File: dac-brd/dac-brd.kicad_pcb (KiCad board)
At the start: 2 copper layers, 51 x 53 mm, 19 parts, among them J1 HTR, J2 I2C, J3 UART, U1 REF5030ID, U2 DAC5578xPW, U3 DAC5578xPW

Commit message: Modified DAC, AMP v2 and Mezzanine to support AMP v3. Finished AMP v3 design.
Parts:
- U1: value REF5030ID -> REF5020ID
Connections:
- net /LED_PWM renamed /EN
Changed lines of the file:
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@@
 	(net 16 "+5V")
 	(net 17 "unconnected-(A1-VSYS-Pad39)")
-	(net 18 "/LED_PWM")
+	(net 18 "/EN")
 	(net 19 "unconnected-(U1-Temp-Pad3)")
 	(net 20 "unconnected-(U1-DNC-Pad1)")
@@
 			(layers "*.Cu" "*.Mask")
 			(remove_unused_layers no)
-			(net 18 "/LED_PWM")
+			(net 18 "/EN")
 			(pinfunction "GPIO17")
 			(pintype "bidirectional")
@@
 			(layers "F.Cu" "F.Mask")
 			(roundrect_rratio 0.5)
-			(net 18 "/LED_PWM")
+			(net 18 "/EN")
 			(pinfunction "GPIO17")
 			(pintype "bidirectional")
@@
 			(layers "*.Cu" "*.Mask")
 			(remove_unused_layers no)
-			(net 18 "/LED_PWM")
+			(net 18 "/EN")
 			(pinfunction "Pin_33")
 			(pintype "passive")
@@
 			)
 		)
-		(property "Value" "REF5030ID"
+		(property "Value" "REF5020ID"
 			(at 0 3.4 90)
 			(layer "F.Fab")
@@
 			)
 		)
-		(property "Description" "3V 0.05% 10mA Low Noise Precision Voltage Reference, SO-8"
+		(property "Description" "2.048V 0.05% 10mA Low Noise Precision Voltage Reference, SO-8"
 			(at 0 0 90)
 			(layer "F.Fab")

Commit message: Final review with Joe
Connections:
- C6 pad 1: +5V -> +3V3
- U1 pad 2: +5V -> +3V3
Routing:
- net +5V: track 46.4 -> 0.00 mm, vias 1 -> 0
- net +3V3: track 28.0 -> 34.5 mm
- net GND: track 4.57 -> 5.79 mm
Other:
- board text added: "EN"
- board text removed: "LED"

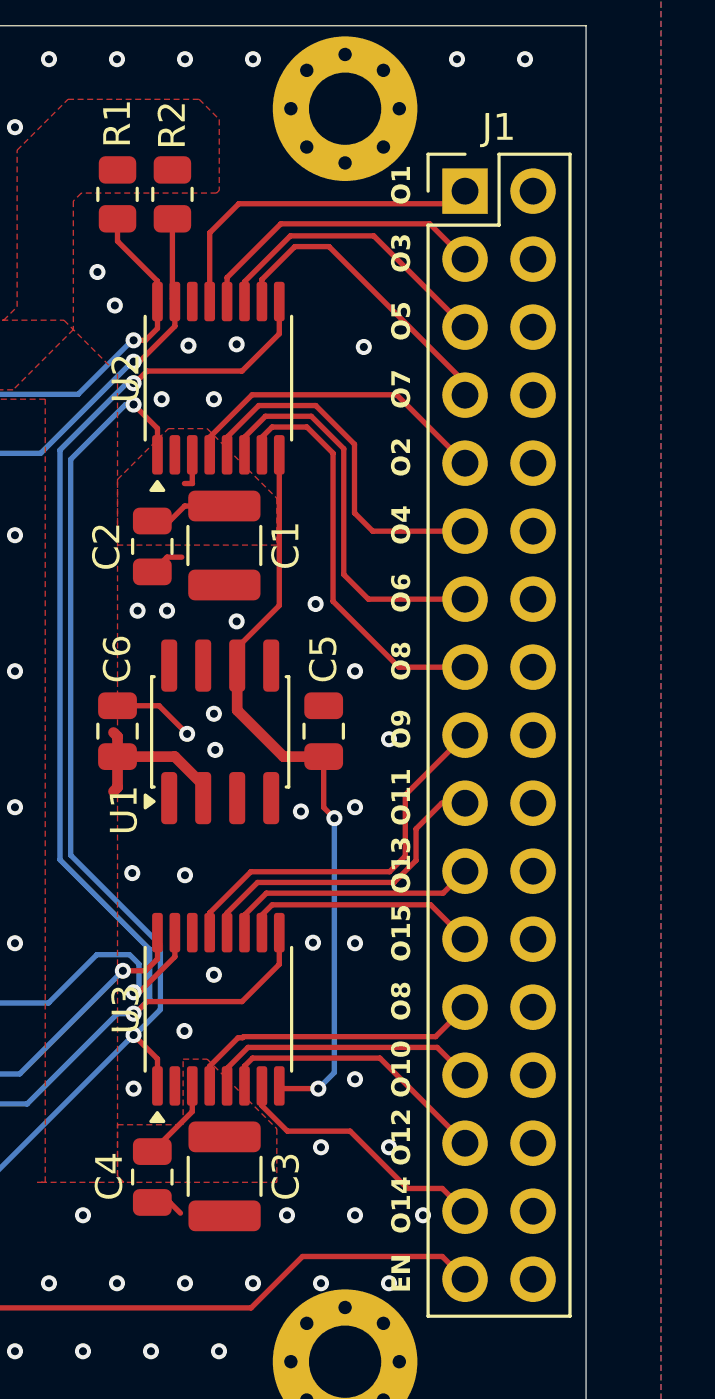
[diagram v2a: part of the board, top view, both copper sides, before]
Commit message: Tested DAC and partially tested INA233
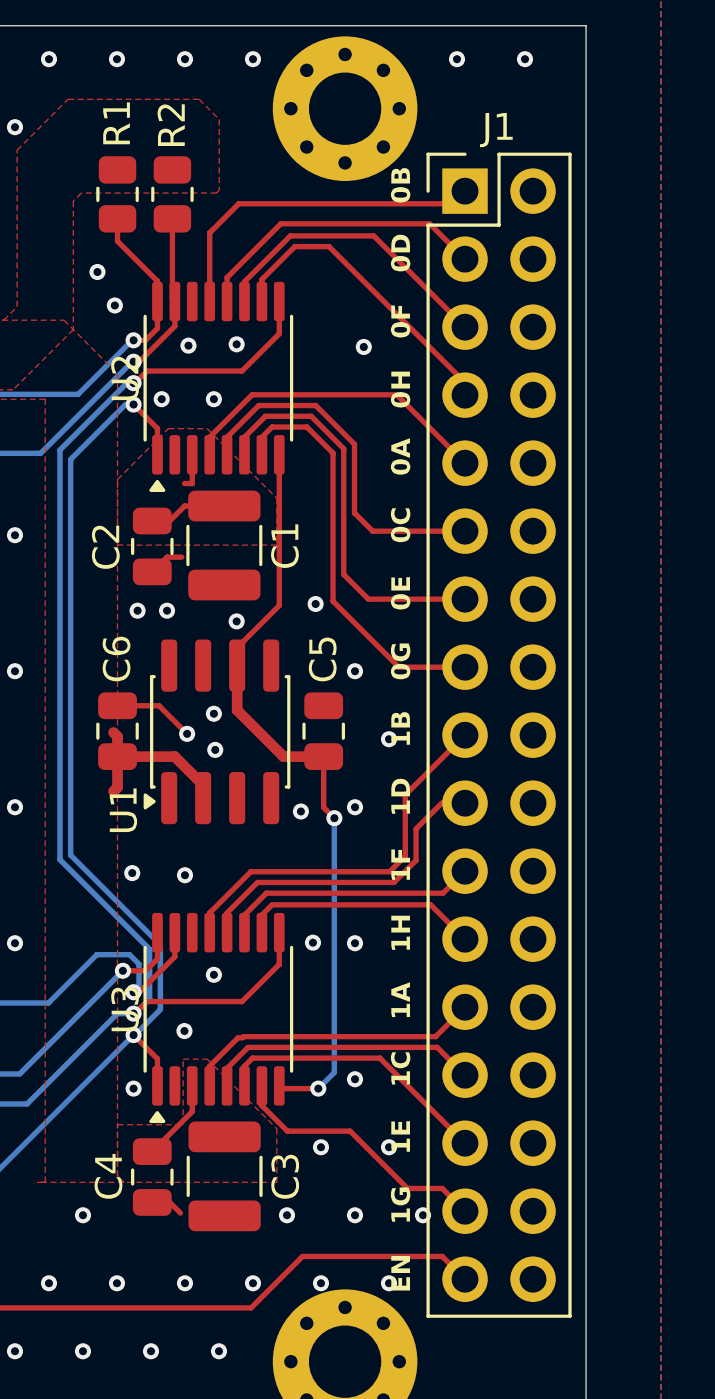
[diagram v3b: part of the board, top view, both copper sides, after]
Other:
- board text added: "0A"
- board text added: "0B"
- board text added: "0C"
- board text added: "0D"
- board text added: "0E"
- board text added: "0F"
- board text added: "0G"
- board text added: "0H"
- board text added: "1A"
- board text added: "1B"
- board text added: "1C"
- board text added: "1D"
- board text added: "1E"
- board text added: "1F"
- board text added: "1G"
- board text added: "1H"
- board text removed: "O1"
- board text removed: "O10"
- board text removed: "O11"
- board text removed: "O12"
- board text removed: "O13"
- board text removed: "O14"
- board text removed: "O15"
- board text removed: "O2"
- board text removed: "O3"
- board text removed: "O4"
- board text removed: "O5"
- board text removed: "O6"
- board text removed: "O7"
- board text removed: "O8"
- board text removed: "O9"

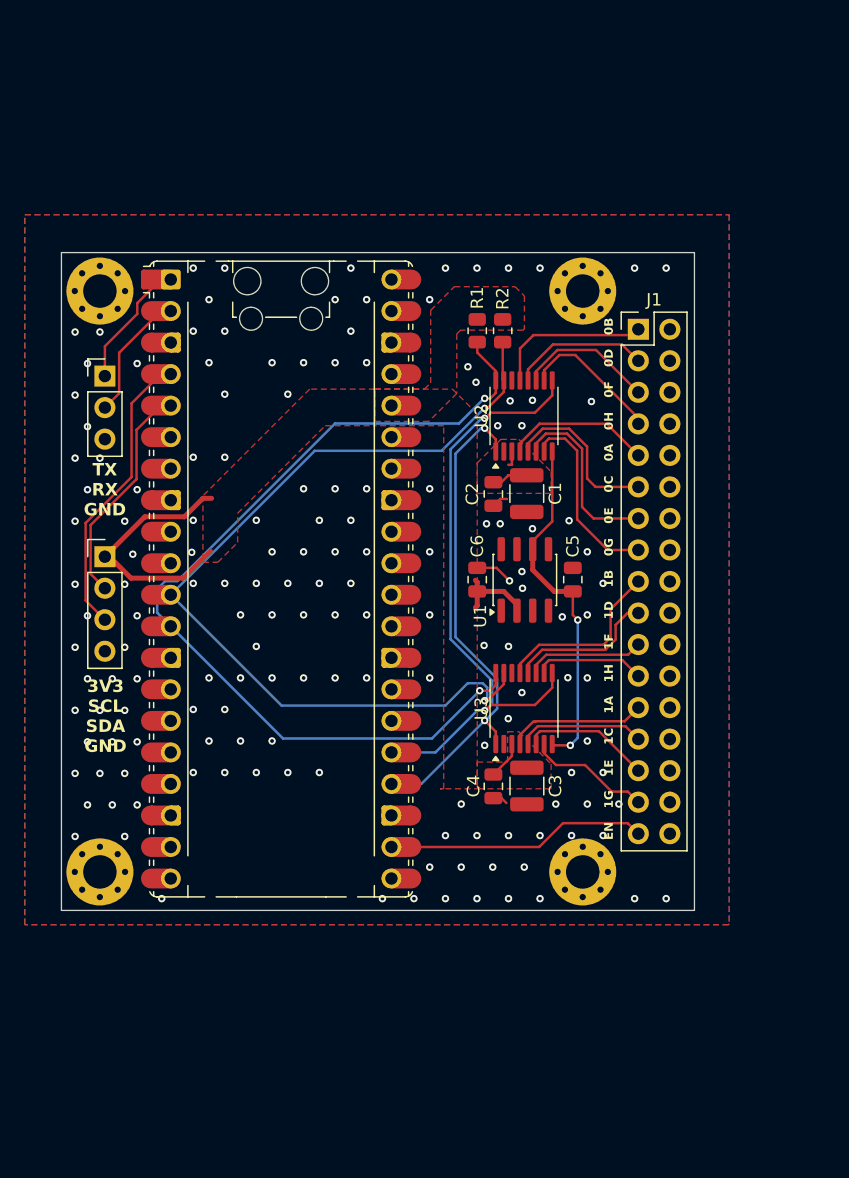
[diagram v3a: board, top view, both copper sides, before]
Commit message: Tested DAC and INA, doing new boards
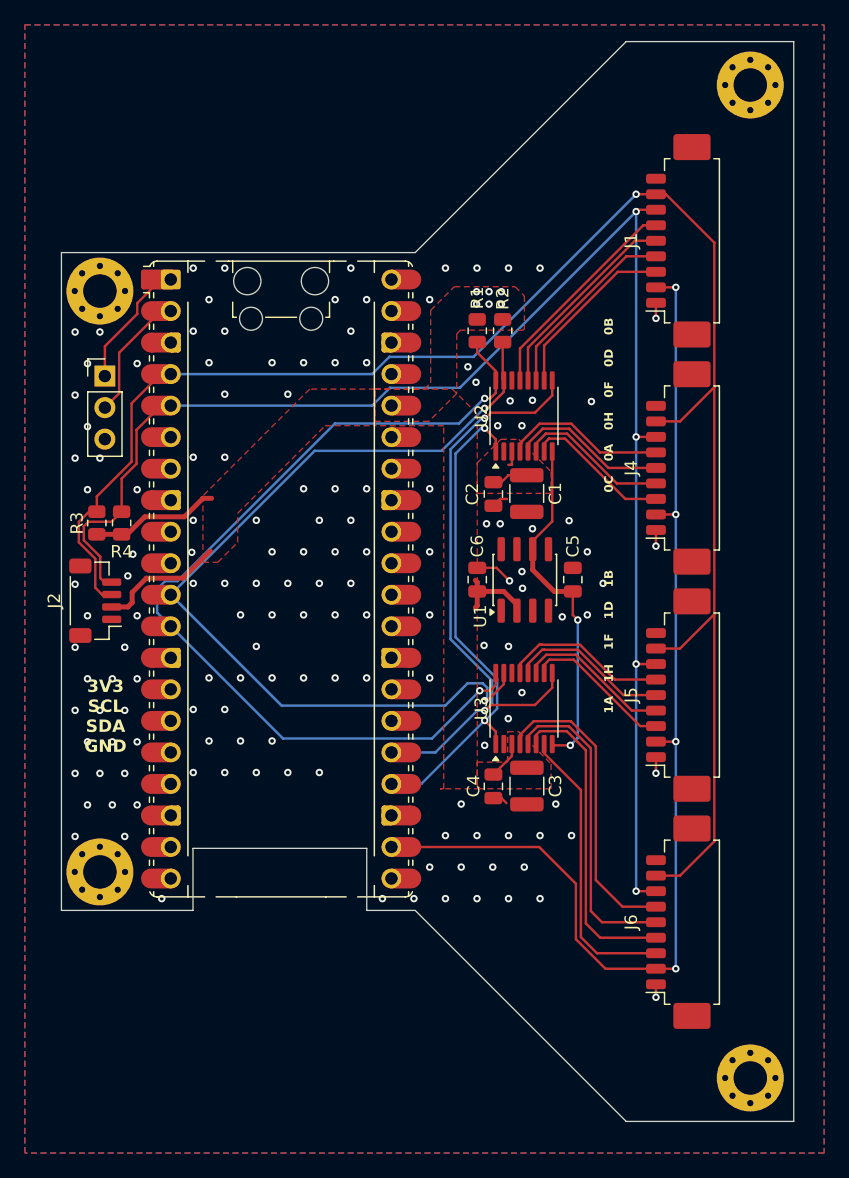
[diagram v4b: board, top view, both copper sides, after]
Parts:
- added J4: STK2, Connector_Molex:Molex_PicoBlade_53261-0971_1x09-1MP_P1.25mm_Horizontal, F.Cu at (183.3, 95.3)
- added J5: STK3, Connector_Molex:Molex_PicoBlade_53261-0971_1x09-1MP_P1.25mm_Horizontal, F.Cu at (183.3, 113.7)
- added J6: STK4, Connector_Molex:Molex_PicoBlade_53261-0971_1x09-1MP_P1.25mm_Horizontal, F.Cu at (183.3, 131.9)
- added R3: 2k, Resistor_SMD:R_0805_2012Metric, F.Cu at (135.8, 99.8)
- added R4: 2k, Resistor_SMD:R_0805_2012Metric, F.Cu at (137.8, 99.8)
- J1: value HTR -> STK1; footprint Connector_PinHeader_2.54mm:PinHeader_2x17_P2.54mm_Vertical -> Connector_Molex:Molex_PicoBlade_53261-0971_1x09-1MP_P1.25mm_Horizontal
- J2: value I2C -> I2C/1Wire; footprint Connector_PinHeader_2.54mm:PinHeader_1x04_P2.54mm_Vertical -> Connector_JST:JST_SH_BM04B-SRSS-TB_1x04-1MP_P1.00mm_Vertical
- moved H3 21.4 mm to (188.5, 144.5)
- moved H4 21.4 mm to (188.5, 64.5)
- moved J1 8.09 mm to (183.3, 77.0), turned to 90 degrees
- moved J2 3.63 mm to (135.7, 106.0), turned to 90 degrees
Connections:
- J1 pad 1: /OUT_1 -> +3V3
- J1 pad 2: GND -> /EN
- J1 pad 3: /OUT_3 -> /OUT_7
- J1 pad 4: GND -> /OUT_5
- J1 pad 5: /OUT_5 -> /OUT_3
- J1 pad 6: GND -> /OUT_1
- J1 pad 7: /OUT_7 -> /SCL1
- J1 pad 8: GND -> /SDA1
- J1 pad 9: /OUT_0 -> GND
- J2 pad 1: +3V3 -> GND
- J2 pad 2: /SCL1 -> +3V3
- J2 pad 4: GND -> /SCL1
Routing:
- net /SDA1: track 22.9 -> 139.6 mm, vias 0 -> 1
- net /SCL1: track 17.5 -> 125.0 mm, vias 0 -> 4
- net /EN: track 21.0 -> 89.2 mm, vias 0 -> 4
- net /OUT_10: track 10.3 -> 25.5 mm
- net /OUT_12: track 10.4 -> 25.6 mm
- net /OUT_8: track 11.2 -> 24.7 mm
- net /OUT_14: track 9.96 -> 23.4 mm
- net /OUT_3: track 11.2 -> 16.5 mm
- net +3V3: track 34.5 -> 39.5 mm, vias 0 -> 10
- net /OUT_1: track 12.7 -> 17.6 mm
- net /OUT_5: track 11.1 -> 15.4 mm
- net /OUT_6: track 15.4 -> 11.8 mm
- net /OUT_15: track 8.93 -> 12.1 mm
- net /OUT_13: track 9.57 -> 12.5 mm
- net /OUT_7: track 11.5 -> 14.3 mm
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- added copper zone on In2.Cu, net +3V3
- added copper zone on In1.Cu, net GND
- added copper zone on In2.Cu, net GND
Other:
- board size 51 x 53 mm -> 59 x 87 mm
- copper layers 2 -> 4
- board text added: "RIGHT ANGLE DEBUG CONN 3 POS 2.54"
- board text removed: "0E"
- board text removed: "0G"
- board text removed: "1C"
- board text removed: "1E"
- board text removed: "1G"
- board text removed: "EN"
- board text removed: "TX RX GND"

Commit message: Updated all boards for production
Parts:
- added H5: ~, MountingHole:MountingHole_2.7mm_M2.5_Pad_Via, F.Cu at (169.0, 75.5)
- added H6: ~, MountingHole:MountingHole_2.7mm_M2.5_Pad_Via, F.Cu at (169.0, 133.5)
- added J7: LED, Connector_Molex:Molex_PicoBlade_53398-0271_1x02-1MP_P1.25mm_Vertical, F.Cu at (136.6, 118.9)
- H1, H2, H3, H4: value MountingHole_Pad -> ~
- J3: renamed from J1; footprint Connector_Molex:Molex_PicoBlade_53261-0971_1x09-1MP_P1.25mm_Horizontal -> Connector_Molex:Molex_PicoBlade_53261-1071_1x10-1MP_P1.25mm_Horizontal
- J4, J5, J6: footprint Connector_Molex:Molex_PicoBlade_53261-0971_1x09-1MP_P1.25mm_Horizontal -> Connector_Molex:Molex_PicoBlade_53261-1071_1x10-1MP_P1.25mm_Horizontal
- moved J6 2.10 mm to (183.3, 134.1)
- moved J3 2.10 mm to (183.3, 75.0)
- moved J4 0.70 mm to (183.3, 94.7)
- moved J5 0.70 mm to (183.3, 114.3)
- moved H3 0.25 mm to (188.7, 144.7)
- moved H4 0.25 mm to (188.7, 64.3)
- moved H1 0.20 mm to (136.1, 81.3)
- moved H2 0.20 mm to (136.1, 127.7)
- renumbered J2 to J1, J3 to J2
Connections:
- A1 pad 16: unconnected-(A1-GPIO12-Pad16)_1 -> /LED
- J3 pad 7: /SCL1 -> /SDA1
- J3 pad 8: /SDA1 -> /SCL1
- J4 pad 7: /SCL1 -> /SDA1
- J4 pad 8: /SDA1 -> /SCL1
- J4 pad 9: GND -> +3V3
- J5 pad 7: /SCL1 -> /SDA1
- J5 pad 8: /SDA1 -> /SCL1
- J5 pad 9: GND -> /SDA1
- J6 pad 7: /SCL1 -> /SDA1
- J6 pad 8: /SDA1 -> /SCL1
- J6 pad 9: GND -> /SCL1
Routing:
- net /SDA1: track 139.6 -> 159.2 mm
- net /SCL1: track 125.0 -> 136.7 mm
- net /EN: track 89.2 -> 95.3 mm
- net /OUT_14: track 23.4 -> 28.6 mm
- net /OUT_8: track 24.7 -> 28.2 mm
- net /LED: track 0.00 -> 3.17 mm
- net /OUT_12: track 25.6 -> 28.5 mm
- net /OUT_3: track 16.5 -> 19.4 mm
- net /OUT_1: track 17.6 -> 20.5 mm
- net /OUT_10: track 25.5 -> 28.4 mm
- net /OUT_5: track 15.4 -> 18.2 mm
- net /OUT_7: track 14.3 -> 17.1 mm
- net +3V3: track 39.5 -> 41.4 mm, vias 10 -> 14
- net /OUT_15: track 12.1 -> 13.9 mm
- net /OUT_13: track 12.5 -> 14.1 mm
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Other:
- board size 59 x 87 mm -> 59.5 x 87 mm
- board text added: "${PRJ_TITLE} Rev.${BOARD_REV}"
- board text added: "Designer: ${DESIGNER} Reviwer: ${REVIEWER}"
- board text added: "G"
- board text added: "I2C 1-WIRE"
- board text added: "LED"
- board text added: "PIC-D HTR DAC Rev. ${BOARD_REV}"
- board text added: "RX"
- board text added: "STK0 0x40-0x43"
- board text added: "STK1 0x44-0x47"
- board text added: "STK2 0x48-0x4B"
- board text added: "STK3 0x4C-0x4F"
- board text added: "TX"
- board text removed: "0A"
- board text removed: "0B"
- board text removed: "0C"
- board text removed: "0D"
- board text removed: "0F"
- board text removed: "0H"
- board text removed: "1A"
- board text removed: "1B"
- board text removed: "1D"
- board text removed: "1F"
- board text removed: "1H"
- board text removed: "3V3 SCL SDA GND"

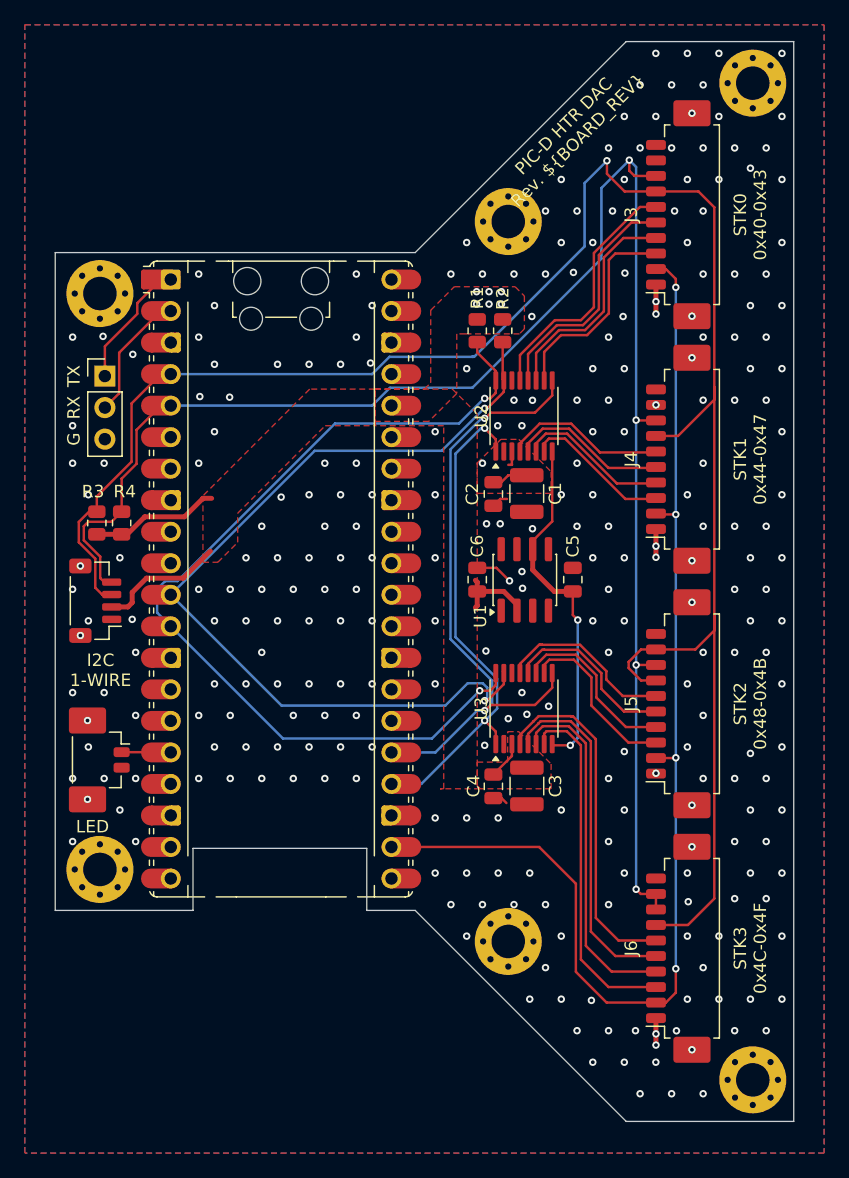
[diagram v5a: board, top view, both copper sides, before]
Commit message: Updated dac-brd connectors to vertical
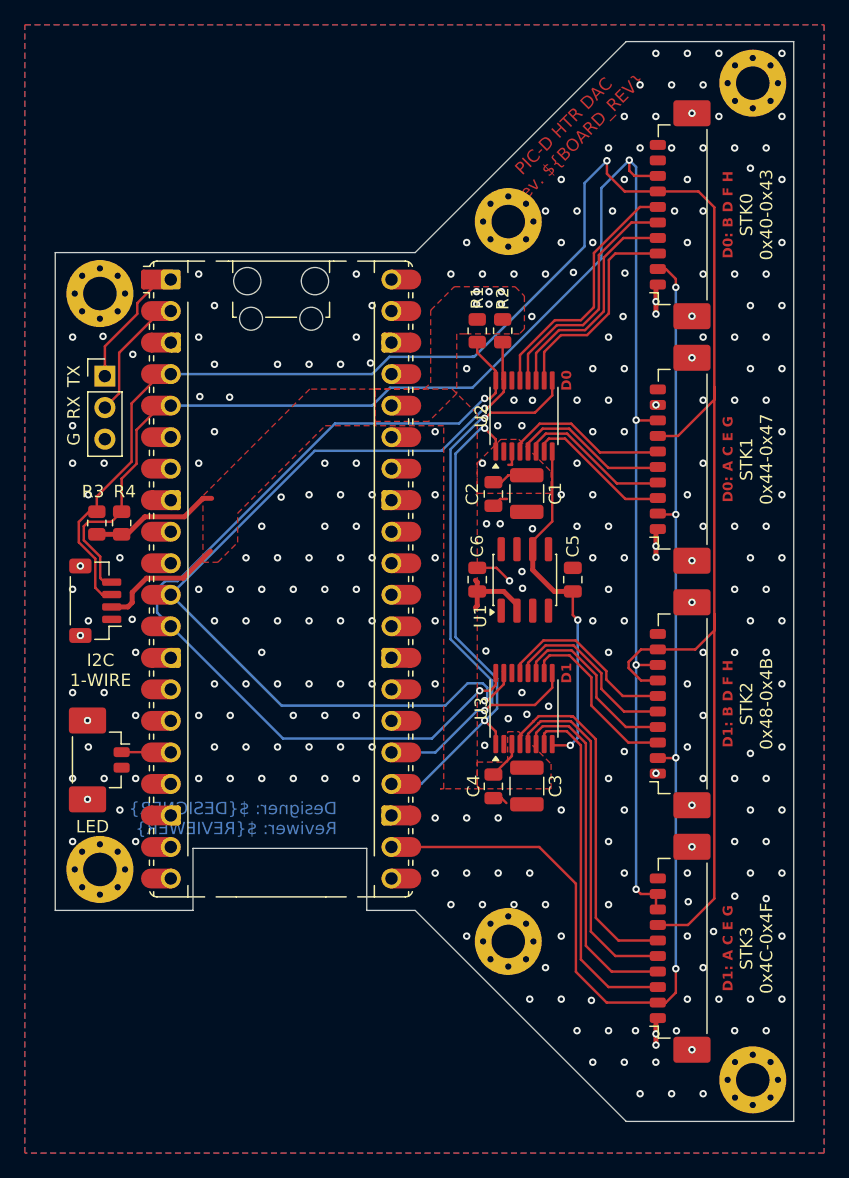
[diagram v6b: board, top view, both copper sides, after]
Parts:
- J3, J4, J5, J6: footprint Connector_Molex:Molex_PicoBlade_53261-1071_1x10-1MP_P1.25mm_Horizontal -> Connector_Molex:Molex_PicoBlade_53398-1071_1x10-1MP_P1.25mm_Vertical
- moved J3 1.00 mm to (182.3, 75.0)
- moved J4 1.00 mm to (182.3, 94.7)
- moved J5 1.00 mm to (182.3, 114.3)
- moved J6 1.00 mm to (182.3, 134.1)
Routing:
- net GND: vias 273 -> 272
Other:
- board text added: "D0"
- board text added: "D0: A C E G"
- board text added: "D0: B D F H"
- board text added: "D1"
- board text added: "D1: A C E G"
- board text added: "D1: B D F H"
- board text removed: "U2"
